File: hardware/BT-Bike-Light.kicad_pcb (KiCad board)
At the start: 2 copper layers, 35.1 x 27.5 mm, 39 parts, among them J101 USB_C_Charge_Port, J102 SWD_Header, Q101 DMN3731U-7, SW101 Button, SW102 Button, U101 PAM2808, U102 nPM1300, U103 BT832

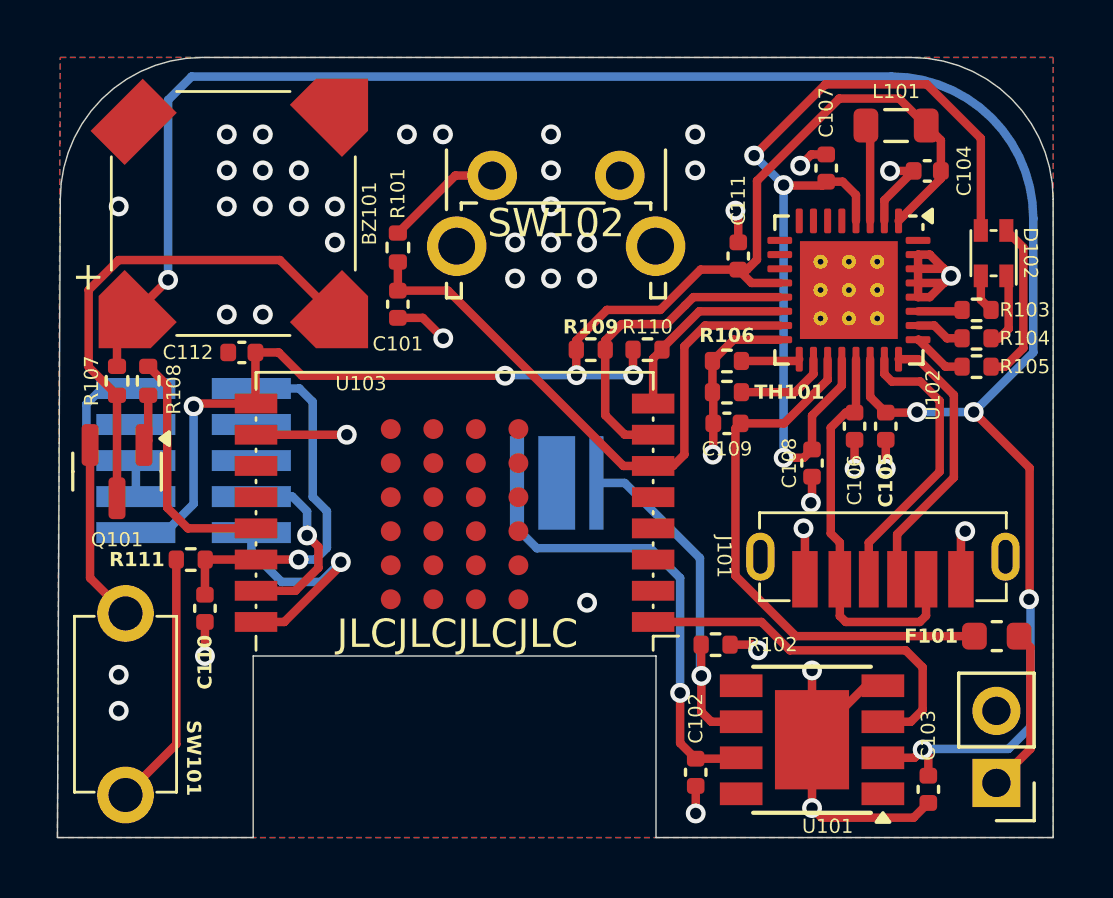
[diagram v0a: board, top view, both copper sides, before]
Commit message: Add accelerometer, replace LED driver, add internal GND layers, fix VSYS routing, update datasheets
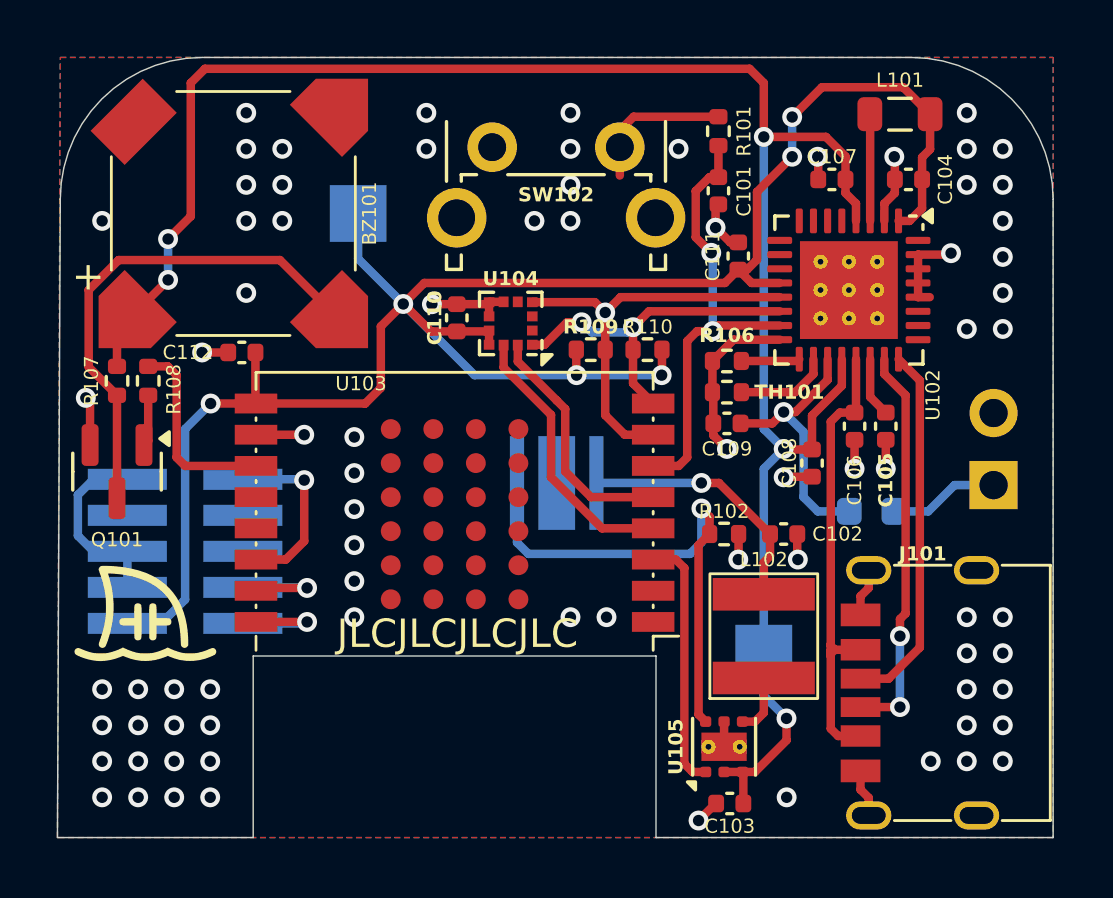
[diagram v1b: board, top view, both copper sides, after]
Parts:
- removed D102: CHRG_LED, Generic_Custom:LED_0606
- removed R103, R104, R105: 110, Resistor_SMD:R_0402_1005Metric
- removed R111: 10K, Resistor_SMD:R_0402_1005Metric
- removed SW101: Button, C&K:PTS636_TH
- removed U101: PAM2808, Package_SO:Diodes_SO-8EP
- added L102: 2.2uH, Generic_Custom:Inductor_3.6x4.1, F.Cu at (149.8, 100.4)
- added TP103: VSYS, TestPoint:TestPoint_Pad_2.0x2.0mm, B.Cu at (149.8, 101.0)
- added TP104: 1V8, TestPoint:TestPoint_Pad_2.0x2.0mm, B.Cu at (135.5, 85.5)
- added U104: LIS2DTW12, Package_LGA:LGA-12_2x2mm_P0.5mm, F.Cu at (140.9, 89.4)
- added U105: TPS92201, Package_SON:WSON-6-1EP_2x2mm_P0.65mm_EP1x1.6mm_ThermalVias, F.Cu at (148.4, 104.3)
- BT101, F101: moved to B.Cu
- C102: value 4.7uF -> 10uH
- G***: moved to F.Cu
- J101: footprint Molex:2171780001 -> CUI-Devices:UJC-HP2-3-SMT-TR
- moved C110 13.6 mm to (139.0, 89.2), turned to 90 degrees
- moved R101 12.0 mm to (148.2, 82.6)
- moved C101 12.0 mm to (148.2, 84.7)
- moved G*** 10.7 mm to (128.0, 99.5), turned to 0 degrees
- moved BT101 10.5 mm to (157.9, 95.1), turned to 0 degrees
- moved C102 8.95 mm to (150.5, 96.8), turned to 0 degrees
- moved C103 7.02 mm to (148.6, 106.3), turned to 180 degrees
- moved F101 6.23 mm to (153.6, 96.0)
- moved J101 4.83 mm to (153.5, 102.4), turned to 90 degrees
- moved R102 3.91 mm to (148.4, 96.8)
- moved J102 3.21 mm to (127.4, 100.0)
- moved SW102 1.00 mm to (140.2, 83.2)
- moved C104 0.73 mm to (154.9, 84.3)
- moved C107 0.45 mm to (152.2, 84.3), turned to 180 degrees
- moved L101 0.42 mm to (154.6, 82.0)
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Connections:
- BZ101 pad 1: VBUSOUT -> VSYS
- C103 pad 1: VBUSOUT -> VSYS
- C110 pad 1: /nRST -> +1V8
- R107 pad 1: VBUSOUT -> VSYS
- SW102 pad 1: Net-(R101-Pad2) -> GND
- SW102 pad 2: GND -> Net-(R101-Pad2)
- U103 pad 1: /LED_EN -> unconnected-(U103-P026-Pad1)
- U103 pad 11: unconnected-(U103-P013-Pad11) -> /BUZZER
- U103 pad 13: /BUZZER -> unconnected-(U103-P020-Pad13)
- U103 pad 3: unconnected-(U103-P000-Pad3) -> /LED_EN
- U103 pad 4: unconnected-(U103-P001-Pad4) -> /ACCEL_INT2
- U103 pad 5: unconnected-(U103-P002-Pad5) -> /ACCEL_INT1
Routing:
- net VBUSOUT: track 75.2 -> 2.11 mm, vias 5 -> 0
- net VSYS: track 32.6 -> 69.8 mm, vias 3 -> 5
- net +1V8: track 49.5 -> 71.1 mm, vias 4 -> 6
- net GND: track 57.7 -> 38.3 mm, vias 46 -> 78
- net /VBAT_FUSE: track 19.3 -> 9.54 mm, vias 0 -> 1
- net /ACCEL_INT2: track 0.00 -> 9.70 mm
- net Net-(R111-Pad2): track 9.04 -> 0.00 mm
- net /ACCEL_INT1: track 0.00 -> 8.62 mm
- net Net-(D101-A): track 16.3 -> 9.08 mm
- net /nRST: track 13.4 -> 6.30 mm
- net Net-(D102-RK): track 5.81 -> 0.00 mm
- net /SCL: track 6.76 -> 12.5 mm, vias 0 -> 2
- net Net-(D101-K): track 12.8 -> 18.0 mm
- net /BTN: track 21.3 -> 16.2 mm, vias 0 -> 2
- net /SWDIO: track 8.49 -> 4.09 mm
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- added copper zone on In1.Cu, net GND
- added copper zone on In2.Cu, net GND
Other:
- copper layers 2 -> 4

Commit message: PCB cleanup
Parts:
- moved J101 1.60 mm to (155.1, 102.4)
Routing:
- net VBUS: track 16.4 -> 19.6 mm
- net Net-(J101-CC1): track 14.0 -> 14.7 mm
- net GND: vias 78 -> 77

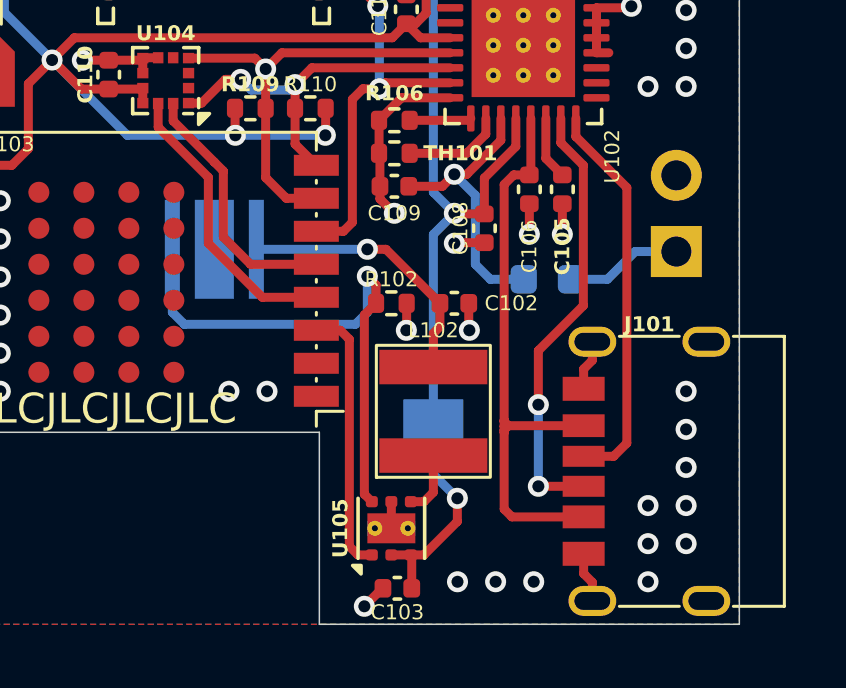
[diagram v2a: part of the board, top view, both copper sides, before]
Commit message: Add LED driver enable signal
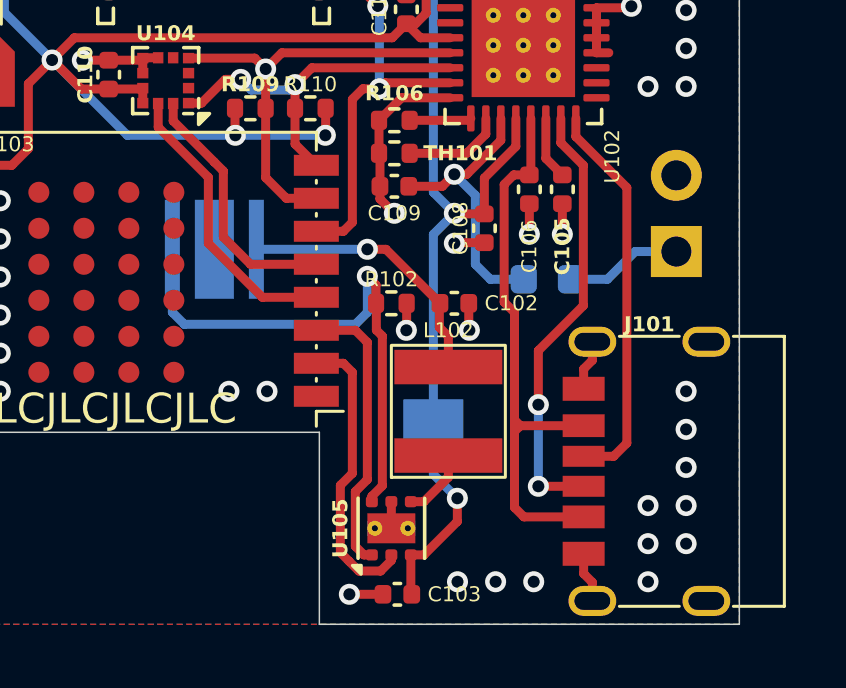
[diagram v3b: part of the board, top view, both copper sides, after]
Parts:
- moved L102 0.50 mm to (150.3, 100.4)
- moved C103 0.20 mm to (148.6, 106.5)
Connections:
- U103 pad 2: unconnected-(U103-P027-Pad2) -> /LED_EN
- U103 pad 3: /LED_EN -> /LED_PWM
- U105 pad 1: /LED_EN -> /LED_PWM
- U105 pad 2: VSYS -> /LED_EN
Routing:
- net /LED_PWM: track 0.00 -> 9.50 mm
- net /LED_EN: track 8.99 -> 9.78 mm

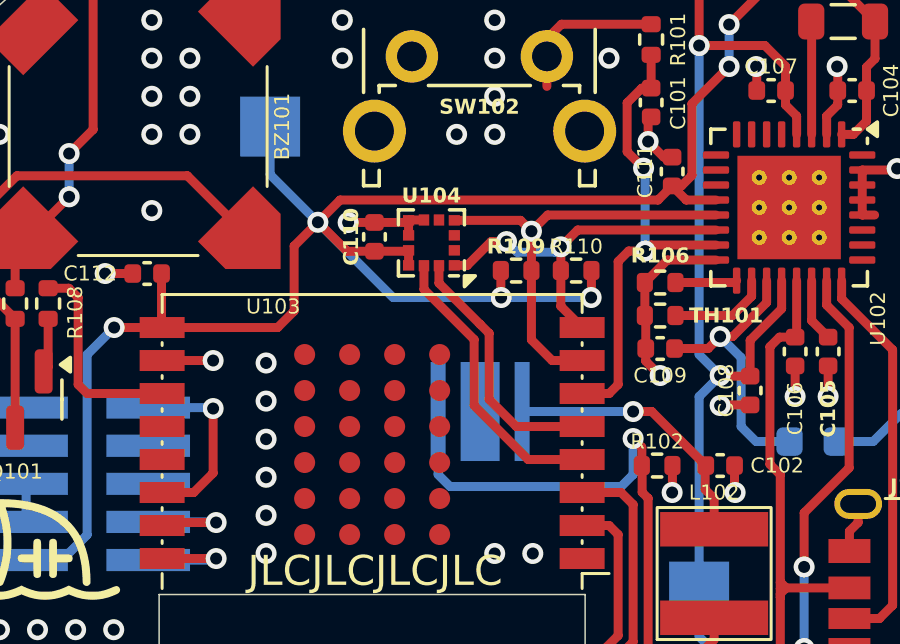
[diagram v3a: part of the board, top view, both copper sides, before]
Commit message: Remove accelerometer
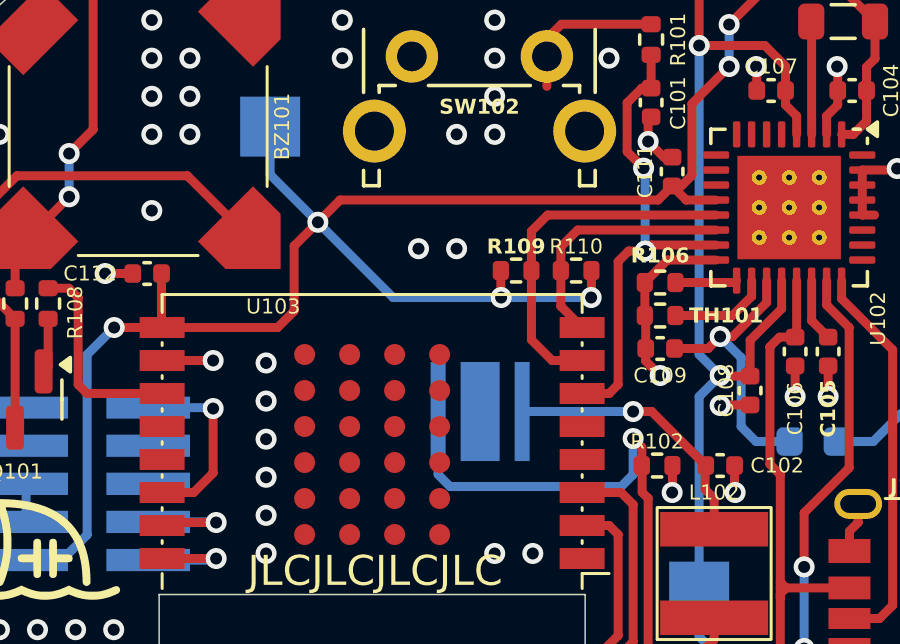
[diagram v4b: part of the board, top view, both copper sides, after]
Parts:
- removed C110: 100nF, Capacitor_SMD:C_0402_1005Metric
- removed U104: LIS2DTW12, Package_LGA:LGA-12_2x2mm_P0.5mm
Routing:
- net /ACCEL_INT2: track 9.70 -> 0.00 mm
- net /ACCEL_INT1: track 8.62 -> 0.00 mm
- net /SCL: track 12.5 -> 8.39 mm, vias 2 -> 0
- net +1V8: track 71.1 -> 67.3 mm
- net GND: track 38.5 -> 35.5 mm, vias 77 -> 78
- net /SDA: track 14.7 -> 12.0 mm, vias 1 -> 0

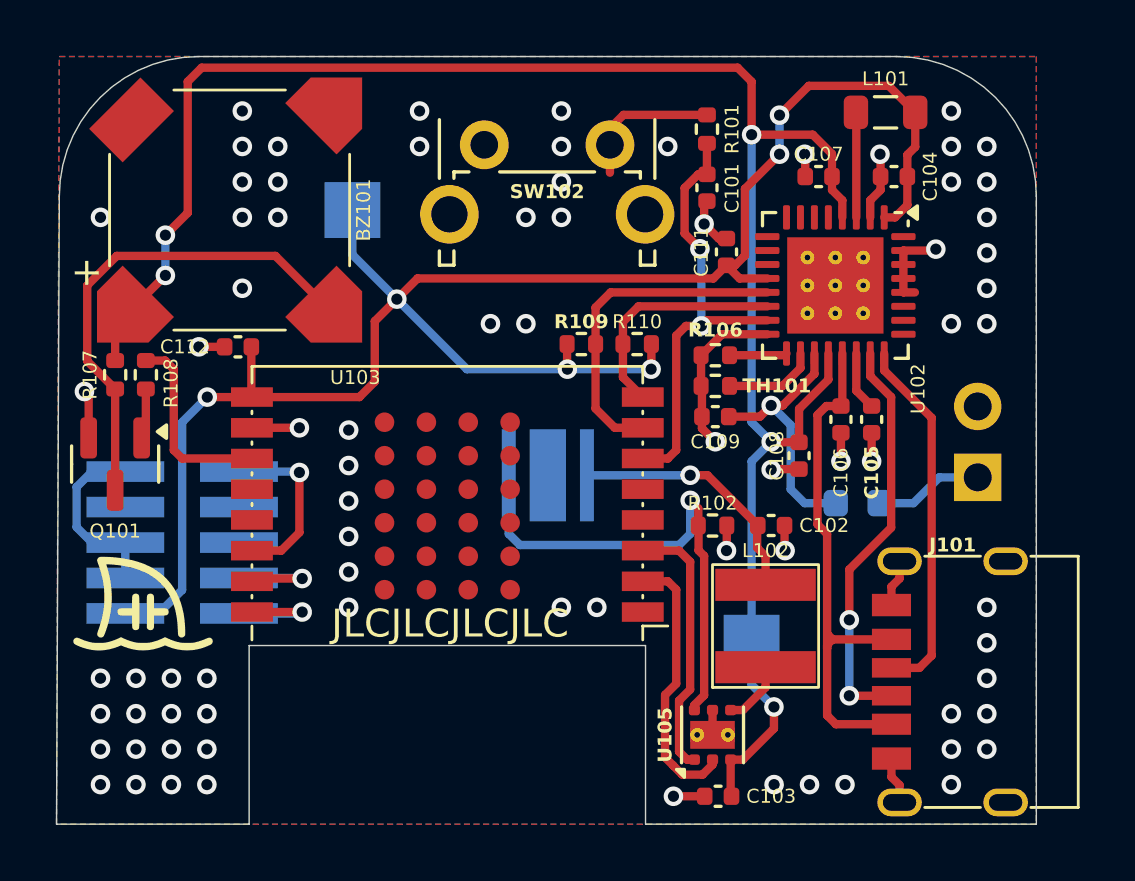
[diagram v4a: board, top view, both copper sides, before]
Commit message: Switch to BT840 (waiting on feedback from radar module supplier before additional changes)
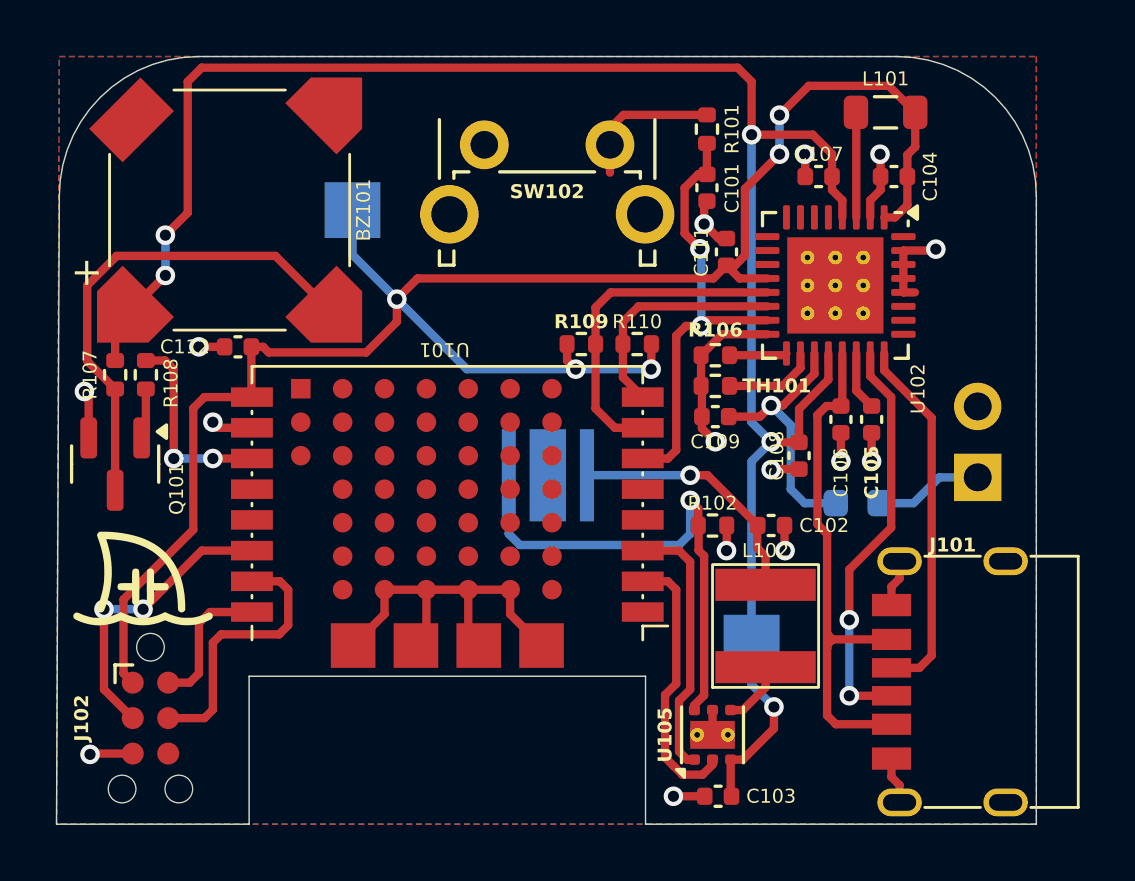
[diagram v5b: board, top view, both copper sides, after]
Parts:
- removed U103: BT832, Fanstel:BT832
- added U101: BT840, Fanstel:BT840, F.Cu at (145.9, 99.9)
- J102: value SWD_Header -> Conn_ARM_SWD_TagConnect_TC2030-NL; footprint Samtech:FTSH-107-01-F-DV-K -> Connector:Tag-Connect_TC2030-IDC-NL_2x03_P1.27mm_Vertical; moved to F.Cu
- moved J102 3.86 mm to (128.3, 103.7), turned to -90 degrees
- moved G*** 0.90 mm to (128.0, 98.6)
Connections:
- J102 pad 3: GND -> /nRST
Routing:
- net GND: track 35.5 -> 43.9 mm, vias 78 -> 15
- net /SWCLK: track 4.11 -> 9.78 mm, vias 1 -> 0
- net /nRST: track 6.30 -> 10.5 mm, vias 1 -> 2
- net /SWDIO: track 4.09 -> 5.10 mm, vias 1 -> 0
- net +1V8: track 67.3 -> 68.0 mm, vias 6 -> 5
- net /BUZZER: track 6.95 -> 7.13 mm, vias 0 -> 2
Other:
- outline, holes or cut-outs redrawn
- board text removed: "JLCJLCJLCJLC"

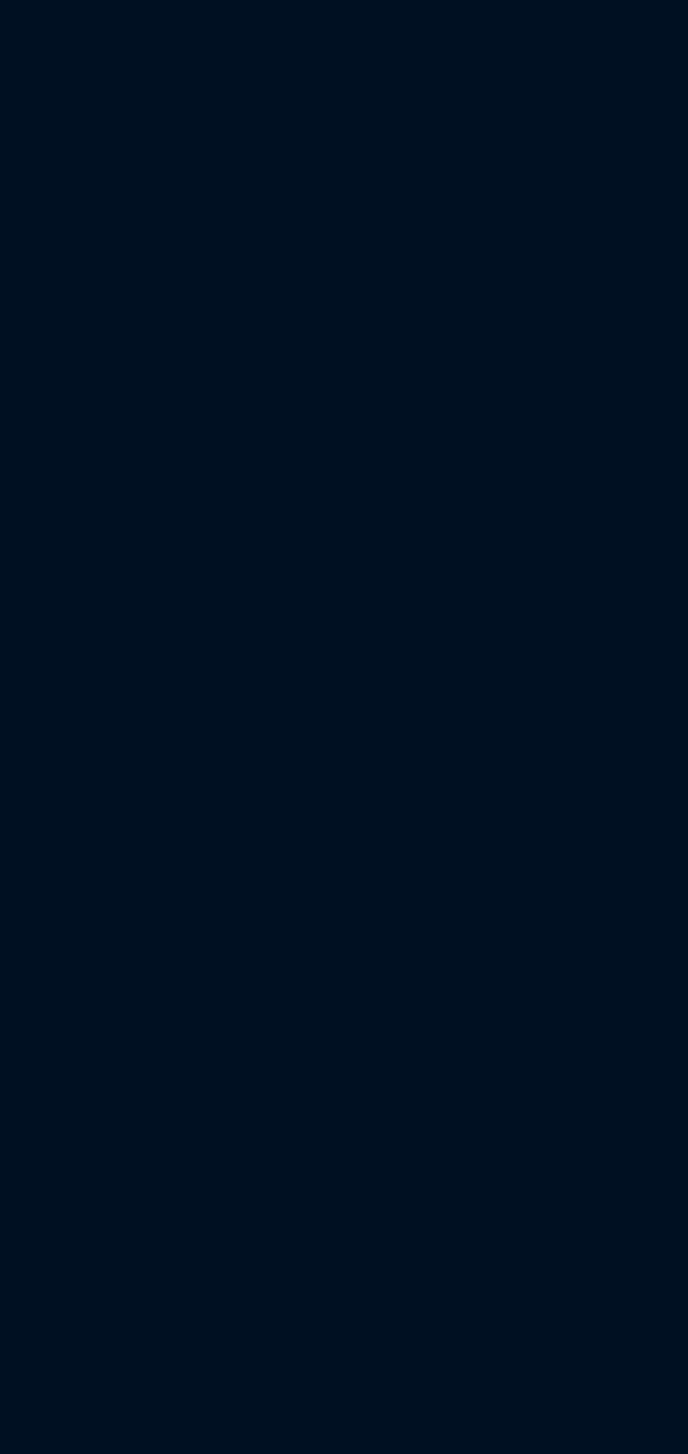
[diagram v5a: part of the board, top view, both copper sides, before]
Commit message: Add radar module to schematic (partially wired)
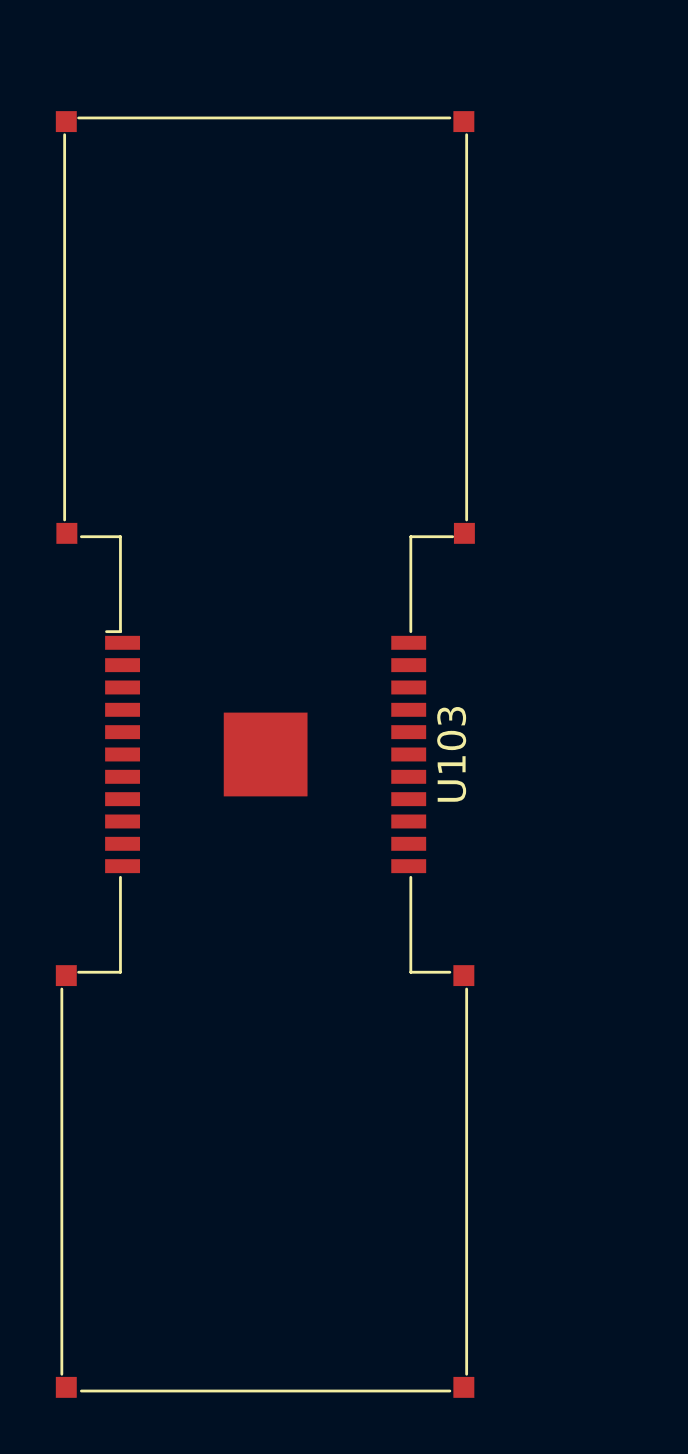
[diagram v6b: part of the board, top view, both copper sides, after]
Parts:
- added U103: FEM11-F09, Terasilic:FEM11-F09, F.Cu at (103.6, 105.0)
